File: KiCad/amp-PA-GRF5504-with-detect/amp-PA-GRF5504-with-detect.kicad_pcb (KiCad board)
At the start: 4 copper layers, 44 x 34 mm, 51 parts, among them J1 142-0701-851, J2 142-0701-851, Q1 P-CH, Q2 N-CH, U2 BDCN-20-13+, U3 LT5534, U4 LT5534, U5 GRF5504

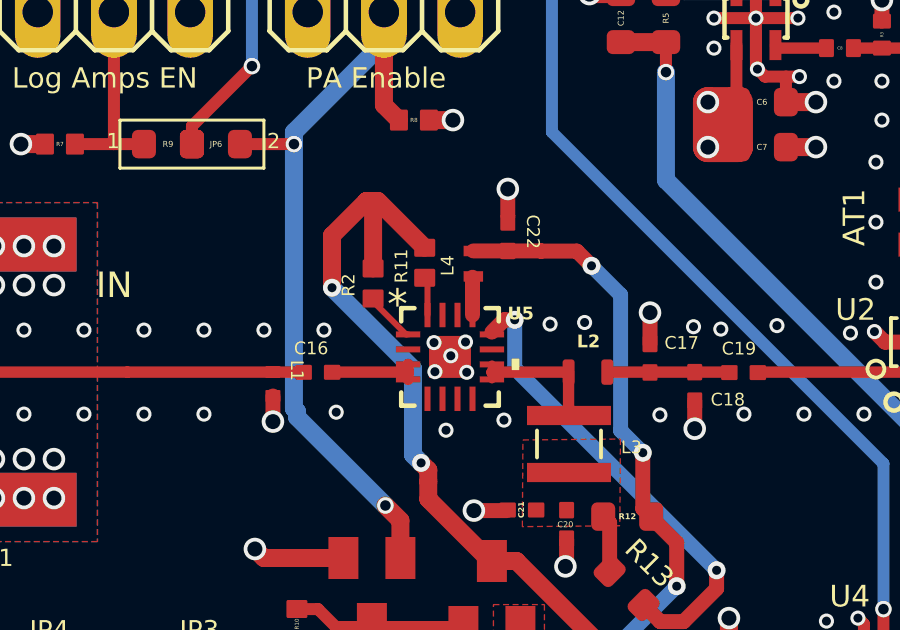
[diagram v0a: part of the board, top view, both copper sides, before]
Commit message: swapped TQP7M9105 chip for GRF5504
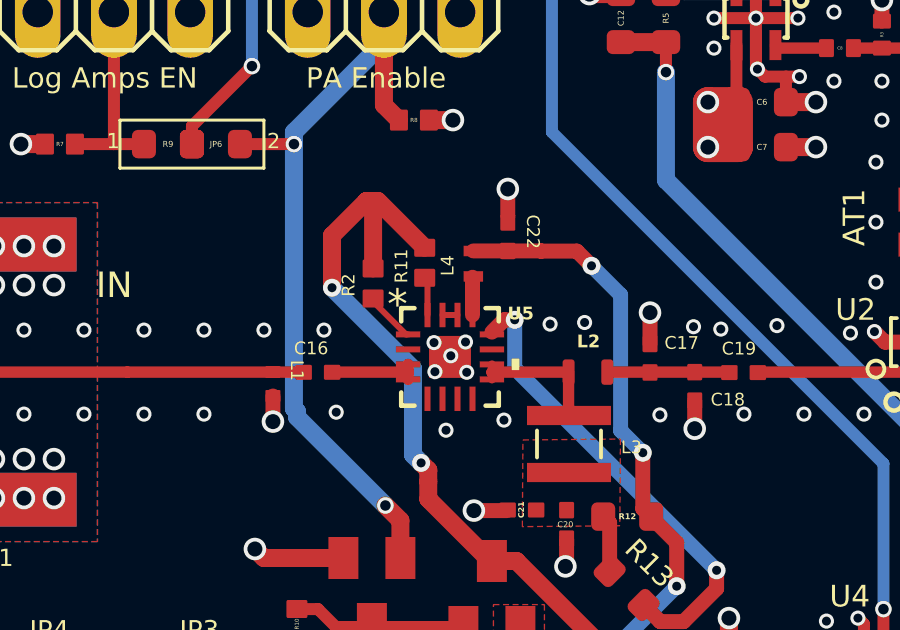
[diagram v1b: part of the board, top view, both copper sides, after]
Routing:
- net GND: track 51.8 -> 52.3 mm
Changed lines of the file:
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@@
 	)
 	(gr_line
-		(start 126.49 143.99)
-		(end 157.29 143.99)
+		(start 126.49 103.99)
+		(end 157.29 103.99)
 		(stroke
 			(width 2)
@@
 		(layer "F.Cu")
 		(net 1)
+	)
+	(segment
+		(start 143.953 102.1)
+		(end 143.453 102.1)
+		(width 0.2)
+		(layer "F.Cu")
+		(net 1)
